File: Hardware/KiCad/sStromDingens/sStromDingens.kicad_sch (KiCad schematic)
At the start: 27 parts, among them J1 LiPo+ (2S-3S), J2 LED, J3 LiPo- (2S-3S), J7 RC, U1 AL8862SP-13, U2 CH32V003J4M6, U3 AMS1117-3.3

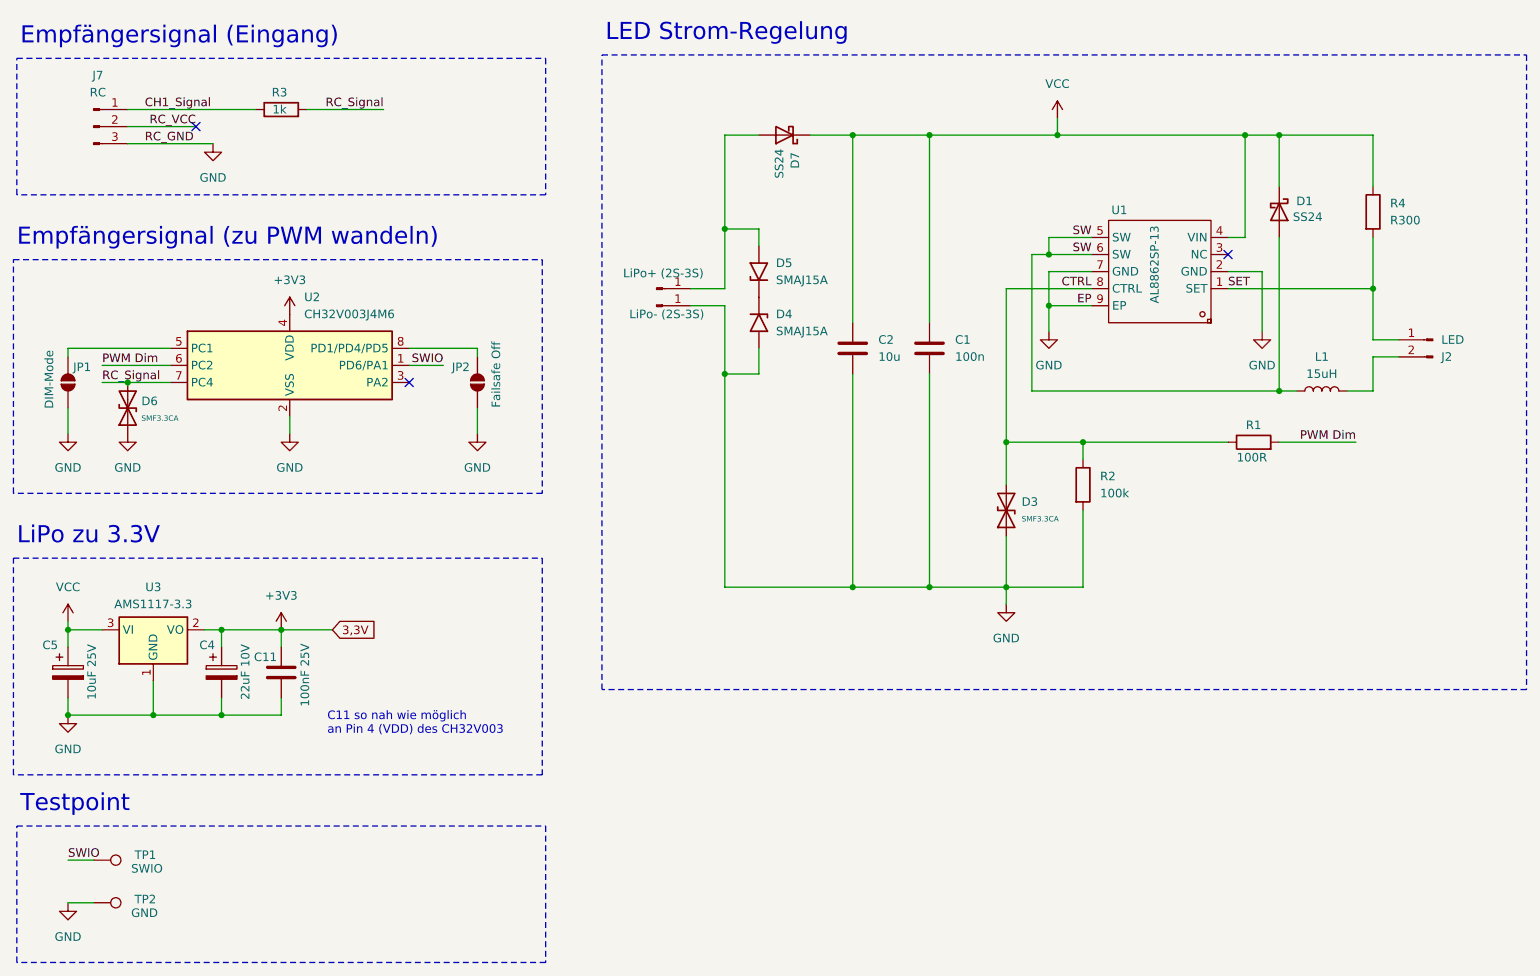
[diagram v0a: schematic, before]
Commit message: Hardware v2.0: Add TVS protection, move Failsafe to Pin 1
- Add SMF3.3CA TVS diodes for input protection (LiPo)
- Add SMAJ26CA TVS diode for LED output protection
- Remove SMAJ15A overvoltage protection
- Move Failsafe jumper from Pin 8 (PD4) to Pin 1 (PD6)
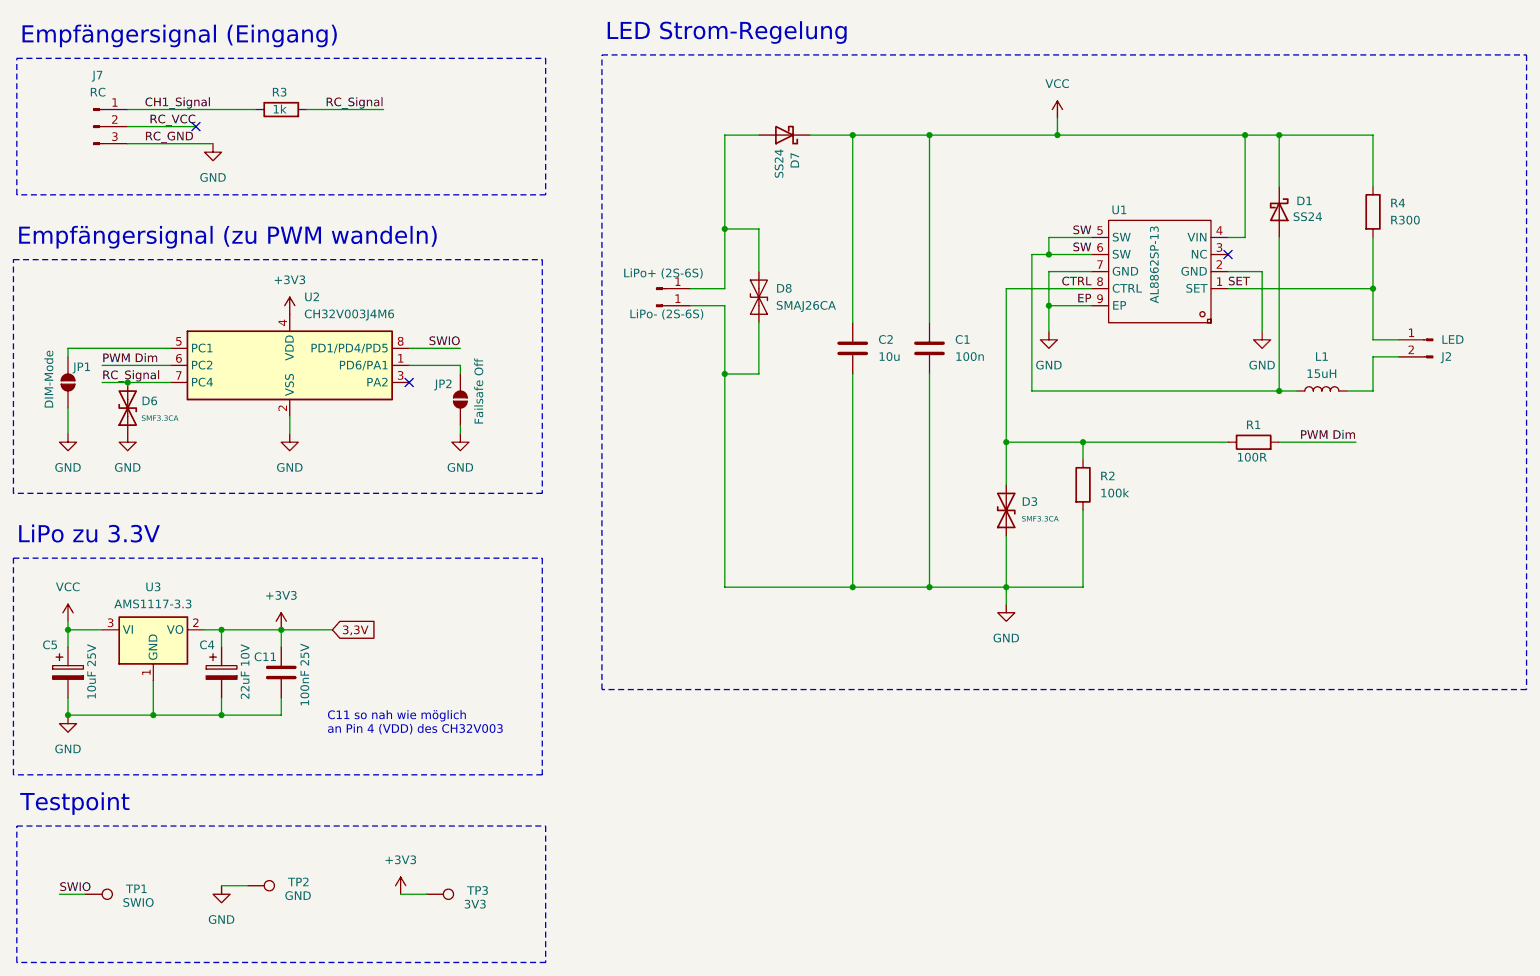
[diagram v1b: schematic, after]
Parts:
- removed D4, D5: SMAJ15A, Diode_SMD:D_SMA, symbol Diode:SMAJ15A
- added D8: SMAJ26CA, Diode_SMD:D_SMB, symbol #partdb:SMAJ26CA
- added TP3: 3V3, TestPoint:TestPoint_Pad_D1.5mm, symbol Connector:TestPoint
- J1: value LiPo+ (2S-3S) -> LiPo+ (2S-6S)
- J3: value LiPo- (2S-3S) -> LiPo- (2S-6S)
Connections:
- net +3V3: now also TP3.1
- net GND: now also D8.2 (A2)
- net SWIO: now also U2.8 (PD1/PD4/PD5); no longer U2.1 (PD6/PA1)
- net at JP2.2 (B): now also U2.1 (PD6/PA1); no longer U2.8 (PD1/PD4/PD5)
- net at D7.2 (A), J1.1 (Pin_1): now also D8.1 (A1)
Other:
- moved on the sheet: JP2, TP1, TP2

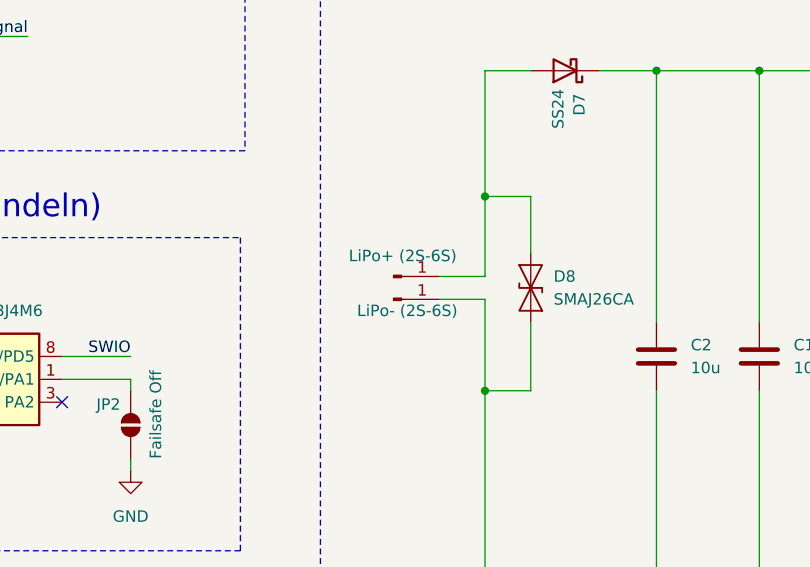
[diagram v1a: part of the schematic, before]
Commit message: Docs/Hardware: LiPo-Spec von 6S auf 4S korrigiert (AMS1117 max. 15V)
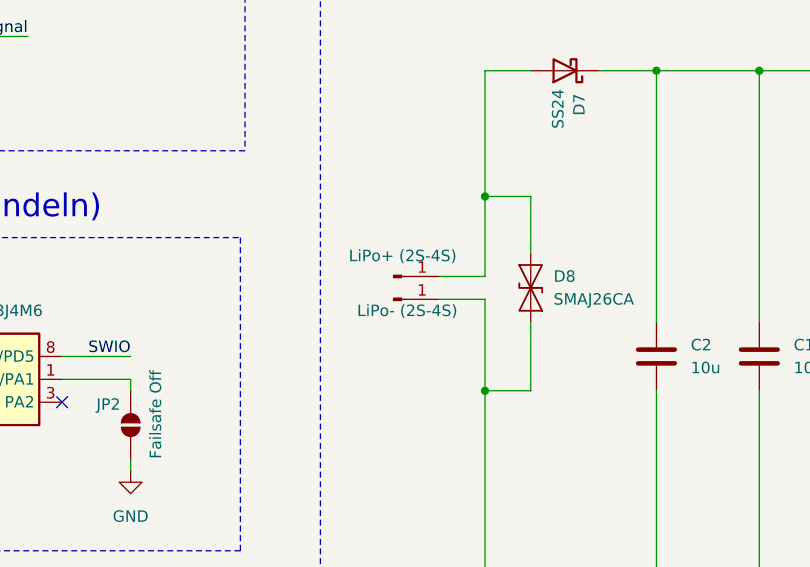
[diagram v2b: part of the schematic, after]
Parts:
- J1: value LiPo+ (2S-6S) -> LiPo+ (2S-4S)
- J3: value LiPo- (2S-6S) -> LiPo- (2S-4S)
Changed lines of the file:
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@@
 			)
 		)
-		(property "Value" "LiPo- (2S-6S)"
+		(property "Value" "LiPo- (2S-4S)"
 			(at 138.684 72.39 0)
 			(effects
@@
 			)
 		)
-		(property "Value" "LiPo+ (2S-6S)"
+		(property "Value" "LiPo+ (2S-4S)"
 			(at 138.176 66.294 0)
 			(effects
